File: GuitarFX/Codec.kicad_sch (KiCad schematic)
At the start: 55 parts, among them IC401 PCM3060PWR, J202 Screw_Terminal_01x02, U401 TLV9161IDBVR, U402 TLV9161IDBVR, U403 TLV9161IDBVR, U406 TLV9161IDBVR, U407 TLV9161IDBVR

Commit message: Finished rough layout
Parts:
- C409: footprint Capacitor_SMD:C_0603_1608Metric -> Capacitor_SMD:C_0402_1005Metric
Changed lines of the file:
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@@
       (effects (font (size 1.27 1.27)))
     )
-    (property "Footprint" "Capacitor_SMD:C_0603_1608Metric" (at 154.6352 62.865 0)
+    (property "Footprint" "Capacitor_SMD:C_0402_1005Metric" (at 154.6352 62.865 0)
       (effects (font (size 1.27 1.27)) hide)
     )

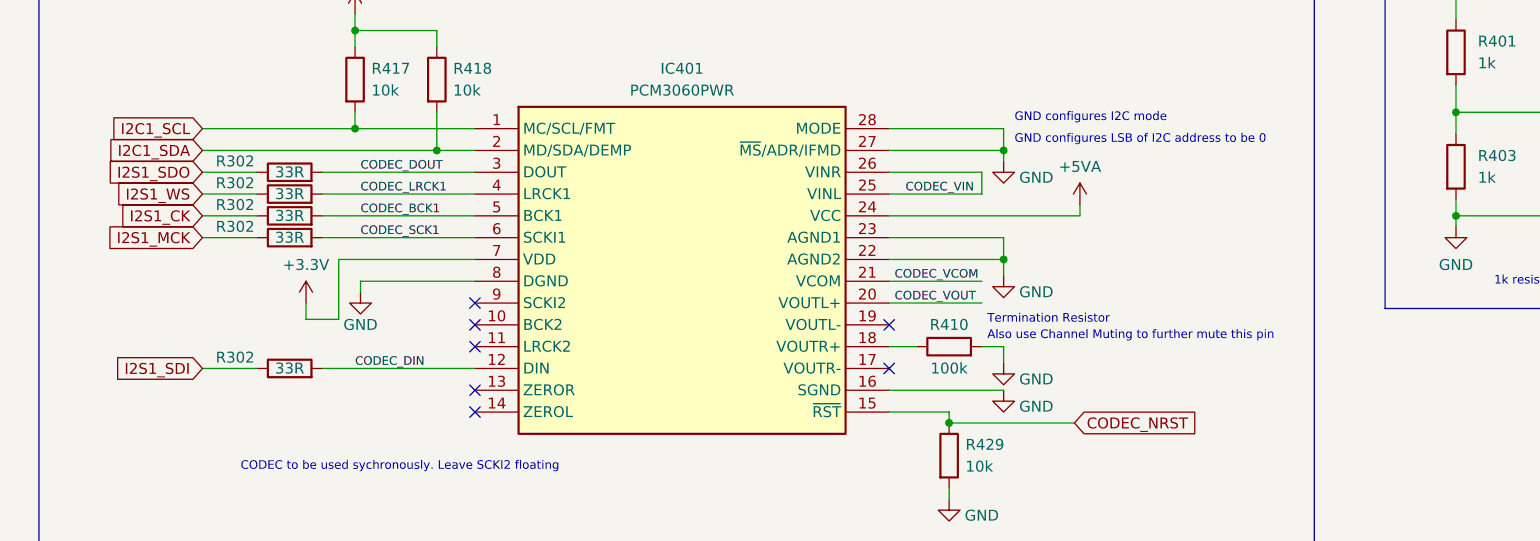
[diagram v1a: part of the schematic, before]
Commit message: Finished routing for i2s
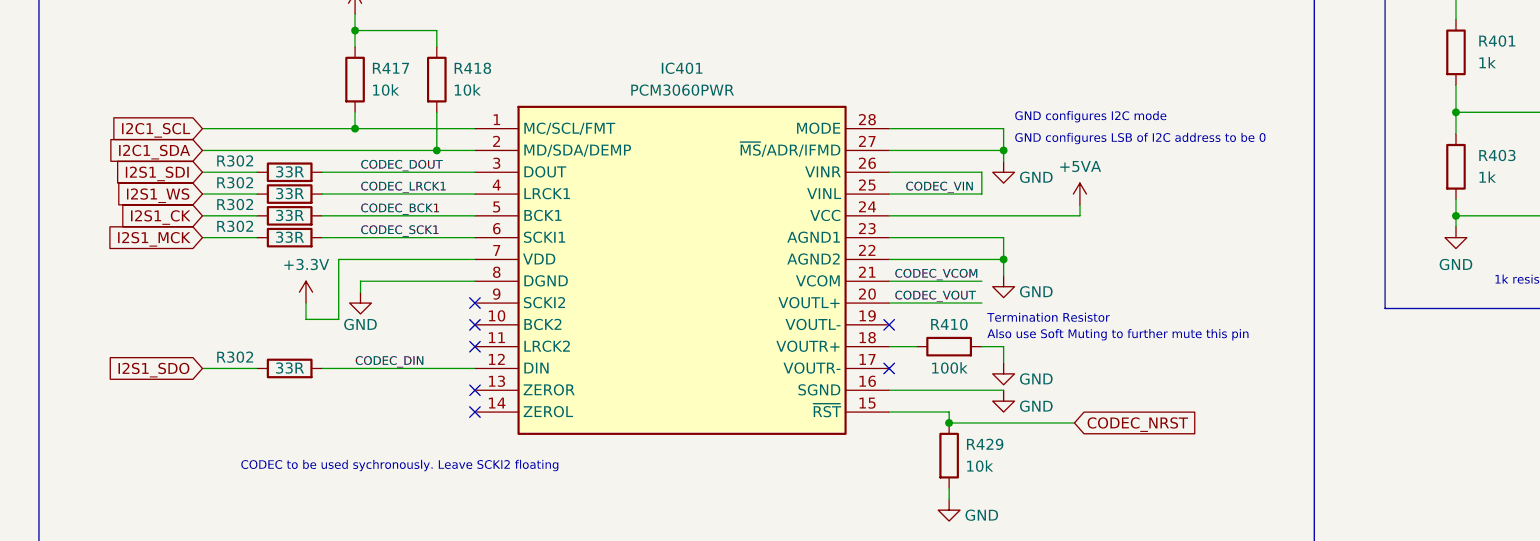
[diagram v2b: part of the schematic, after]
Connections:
- net I2S1_SDI: now also R302.1; no longer R302.1
- net I2S1_SDO: now also R302.1; no longer R302.1
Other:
- note added: "Also use Soft Muting to further mute this pin"
- note removed: "Also use Channel Muting to further mute this pin"
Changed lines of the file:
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@@
     (effects (font (size 1 1)) (justify left bottom))
   )
-  (text "Also use Channel Muting to further mute this pin" (at 128.905 216.535 0)
+  (text "Also use Soft Muting to further mute this pin" (at 128.905 216.535 0)
     (effects (font (size 1 1)) (justify left bottom))
   )
@@
     )
   )
+  (global_label "I2S1_SDI" (shape input) (at 37.465 196.85 180) (fields_autoplaced)
+    (effects (font (size 1.27 1.27)) (justify right))
+    (property "Intersheetrefs" "${INTERSHEET_REFS}" (at 26.1946 196.85 0)
+      (effects (font (size 1.27 1.27)) (justify right) hide)
+    )
+  )
+  (global_label "I2S1_SDO" (shape input) (at 37.465 219.71 180) (fields_autoplaced)
+    (effects (font (size 1.27 1.27)) (justify right))
+    (property "Intersheetrefs" "${INTERSHEET_REFS}" (at 25.4689 219.71 0)
+      (effects (font (size 1.27 1.27)) (justify right) hide)
+    )
+  )
   (global_label "I2C1_SDA" (shape input) (at 37.465 194.31 180) (fields_autoplaced)
     (effects (font (size 1.27 1.27)) (justify right))
@@
     )
   )
-  (global_label "I2S1_SDO" (shape input) (at 37.465 196.85 180) (fields_autoplaced)
-    (effects (font (size 1.27 1.27)) (justify right))
-    (property "Intersheetrefs" "${INTERSHEET_REFS}" (at 25.4689 196.85 0)
-      (effects (font (size 1.27 1.27)) (justify right) hide)
-    )
-  )
   (global_label "I2S1_CK" (shape input) (at 37.465 201.93 180) (fields_autoplaced)
     (effects (font (size 1.27 1.27)) (justify right))
@@
       (effects (font (size 1.27 1.27)) (justify right) hide)
     )
-  )
-  (global_label "I2S1_SDI" (shape input) (at 37.465 219.71 180) (fields_autoplaced)
-    (effects (font (size 1.27 1.27)) (justify right))
-    (property "Intersheetrefs" "${INTERSHEET_REFS}" (at 26.1946 219.71 0)
-      (effects (font (size 1.27 1.27)) (justify right) hide)
-    )

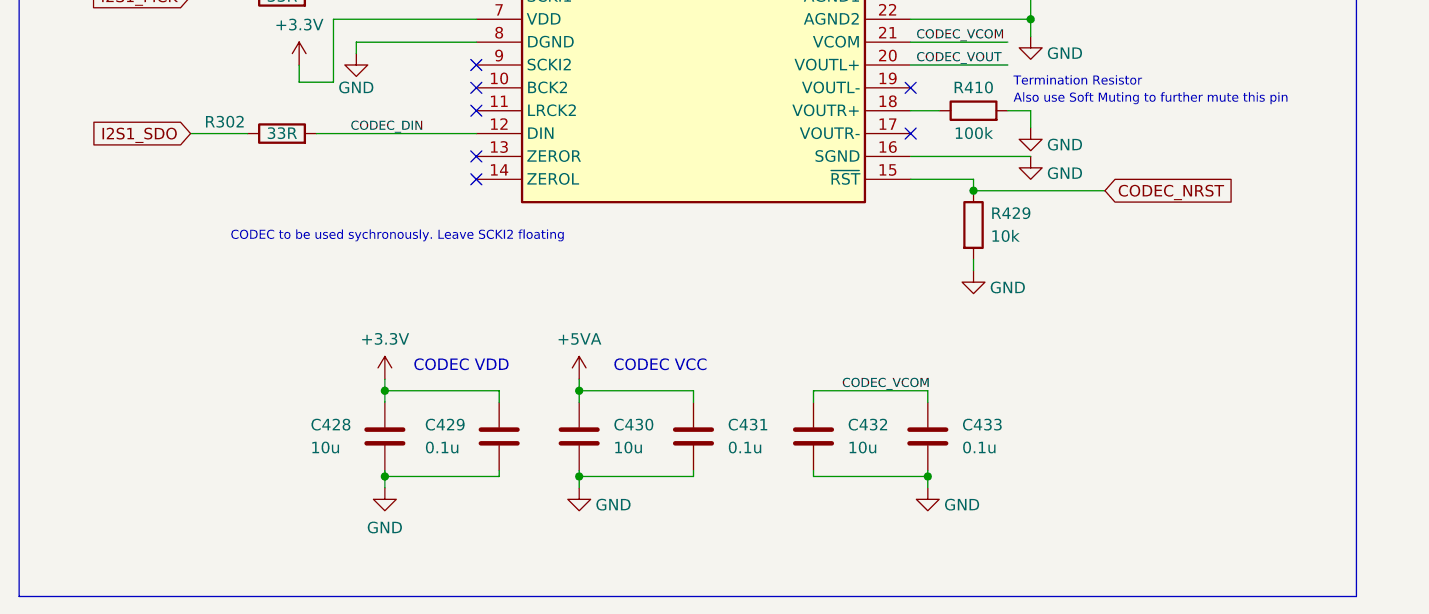
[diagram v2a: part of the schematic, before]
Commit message: Added pi filter for Codec NRST signal
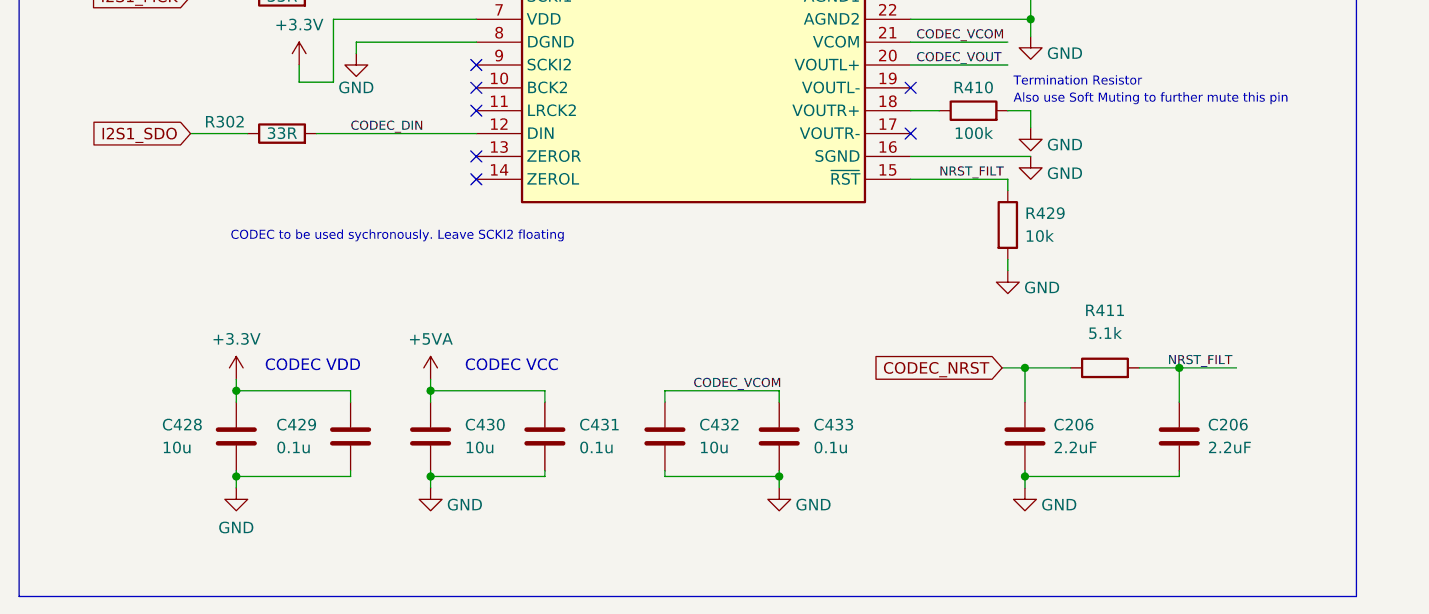
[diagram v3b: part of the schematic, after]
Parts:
- added C206 (x2): 2.2uF, Capacitor_SMD:C_0805_2012Metric, symbol Device:C
- added R411: 5.1k, Resistor_SMD:R_0402_1005Metric, symbol Device:R
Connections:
- net CODEC_NRST: now also C206.1, R411.1; no longer IC401.15 (~{RST}), R429.1
- net GND: now also C206.2, C206.2
- new net NRST_FILT: C206.1, IC401.15 (~{RST}), R411.2, R429.1
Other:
- moved on the sheet: C428, C429, C430, C431, C432, C433, R429

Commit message: Completed ADC terminal block connections. Finished routing
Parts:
- R411: footprint Resistor_SMD:R_0402_1005Metric -> Resistor_SMD:R_0603_1608Metric
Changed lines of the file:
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@@
       (effects (font (size 1.27 1.27)))
     )
-    (property "Footprint" "Resistor_SMD:R_0402_1005Metric" (at 139.065 247.523 90)
+    (property "Footprint" "Resistor_SMD:R_0603_1608Metric" (at 139.065 247.523 90)
       (effects (font (size 1.27 1.27)) hide)
     )

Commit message: Added JLCPCB part numbers for main hardware components to order them
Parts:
- D203: JLCPCB Part# (none) -> C908769
- IC401: JLCPCB Part# (none) -> C2651841
- J202: JLCPCB Part# (none) -> C3029316
- U401, U402, U403, U406, U407: JLCPCB Part# (none) -> C4368955
